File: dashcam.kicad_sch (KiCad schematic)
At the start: 1 part, among them U1 AM6254ATCGHAALW

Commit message: commit++
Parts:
- removed unit 1 of U1
- removed unit 3 of U1
- removed unit 2 of U1
- removed unit 8 of U1
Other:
- added sheet DCAPs (dcaps.kicad_sch)
- added sheet Ethernet (ethernet.kicad_sch)
- added sheet LDO 1V0 (ldo1V0.kicad_sch)
- added sheet PMIC (pmic.kicad_sch)
- added sheet SoC Power (soc_power_sch.kicad_sch)

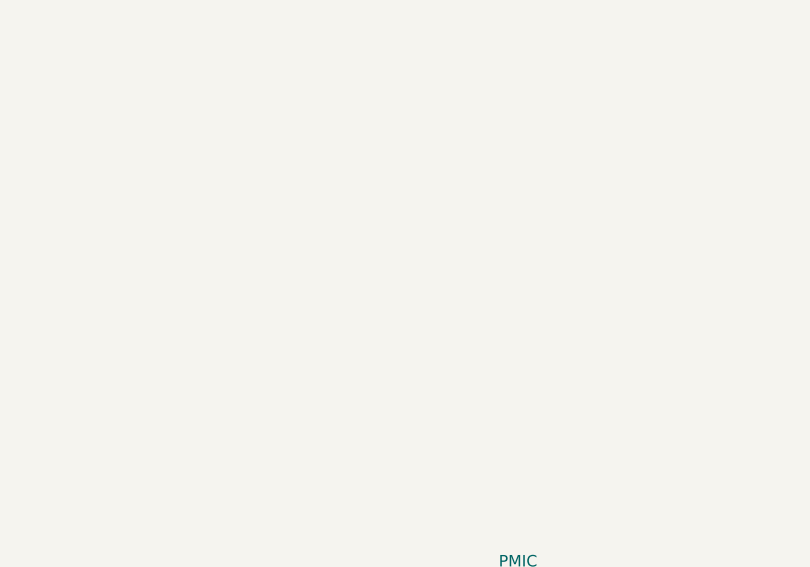
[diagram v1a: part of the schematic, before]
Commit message: SD card changes
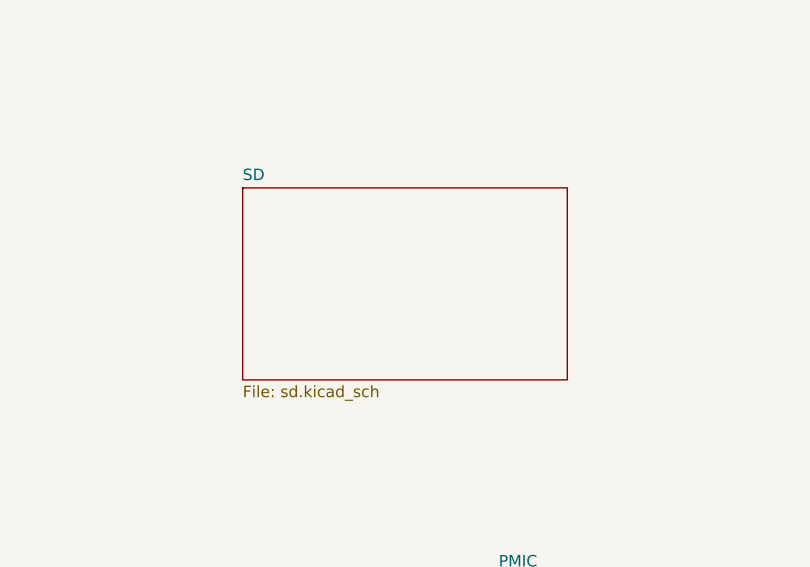
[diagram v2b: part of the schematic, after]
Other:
- added sheet SD (sd.kicad_sch)
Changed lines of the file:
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@@
+	)
+	(sheet
+		(at 123.952 153.924)
+		(size 36.068 21.336)
+		(exclude_from_sim no)
+		(in_bom yes)
+		(on_board yes)
+		(dnp no)
+		(fields_autoplaced yes)
+		(stroke
+			(width 0.1524)
+			(type solid)
+		)
+		(fill
+			(color 0 0 0 0.0000)
+		)
+		(property "Sheetname" "SD"
+			(at 123.952 153.2124 0)
+			(effects
+				(font
+					(size 1.27 1.27)
+				)
+				(justify left bottom)
+			)
+		)
+		(property "Sheetfile" "sd.kicad_sch"
+			(at 123.952 175.8446 0)
+			(effects
+				(font
+					(size 1.27 1.27)
+				)
+				(justify left top)
+			)
+		)
+		(instances
+			(project "dashcam"
+				(path "/30d6913c-7aa4-4f56-9882-2ba08f7e2cce"
+					(page "12")
+				)
+			)
+		)
 	)
 	(sheet

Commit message: Bulk change
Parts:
- removed unit 7 of U1
